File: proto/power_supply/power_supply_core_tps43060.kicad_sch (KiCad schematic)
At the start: 36 parts, among them Q1 BC846, U1 TPS61178, U2 TSV911xxLx

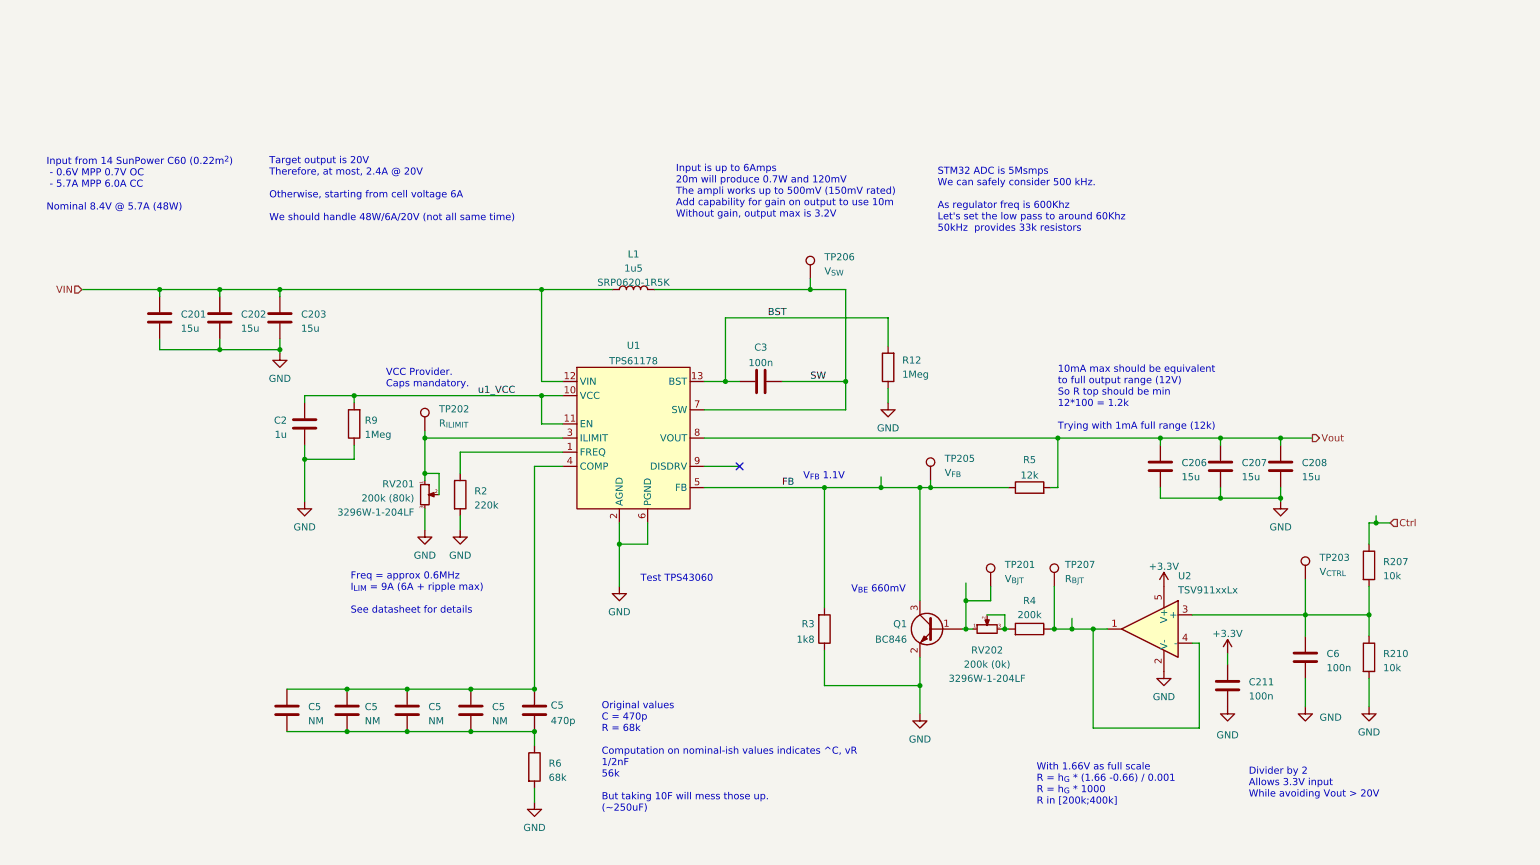
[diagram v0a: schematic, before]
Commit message: Global alimentation update
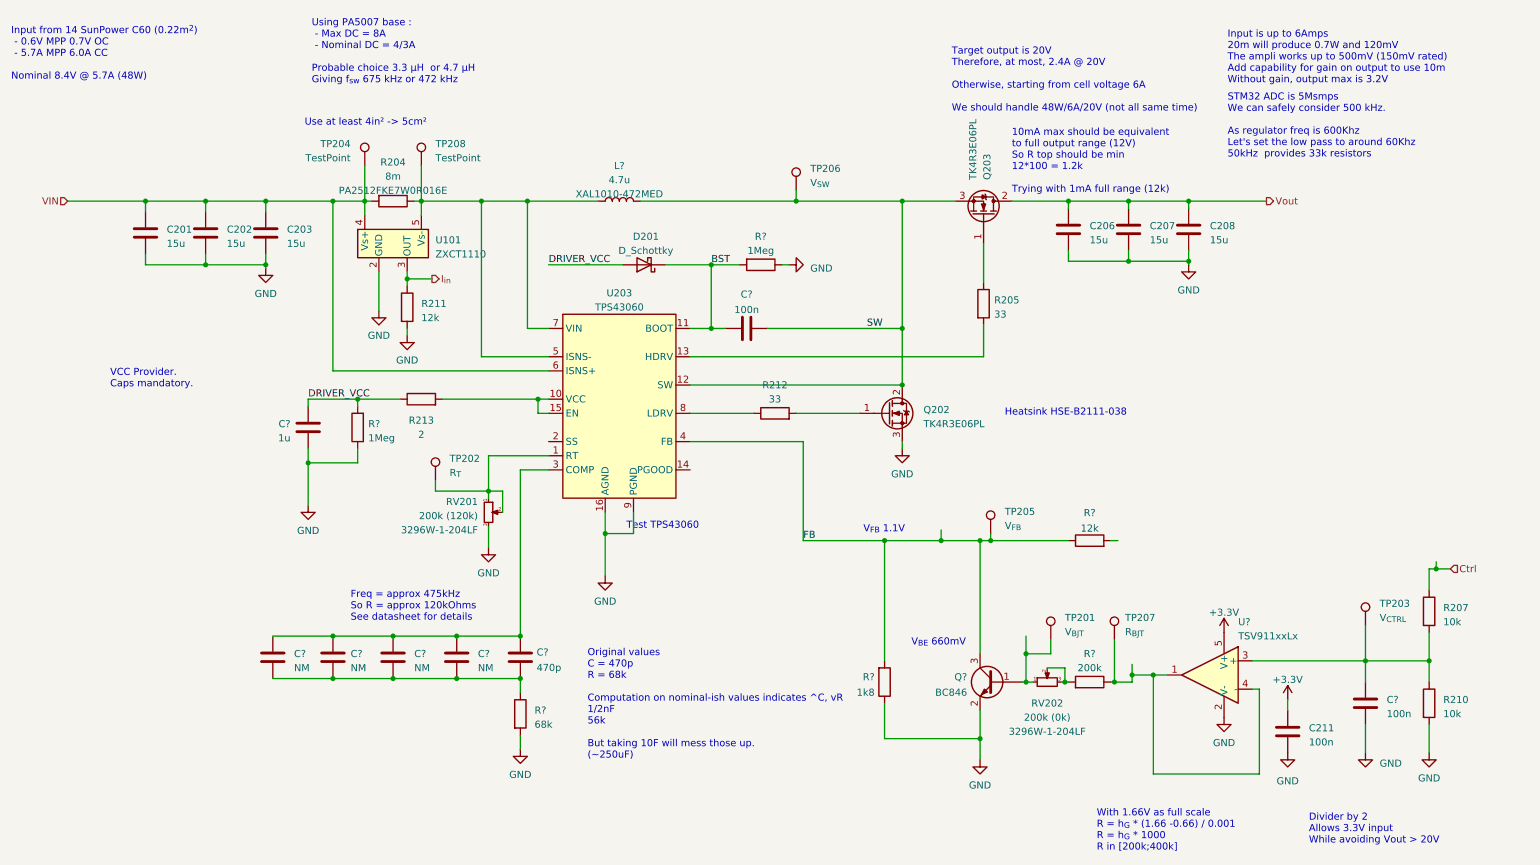
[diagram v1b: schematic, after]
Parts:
- removed R2: 220k, Resistor_SMD:R_0805_2012Metric, symbol Device:R
- removed U1: TPS61178, power_supply:VSON-TPS61178, symbol defis_solaires_4:TPS61178
- added D201: D_Schottky, symbol Device:D_Schottky
- added Q202, Q203: TK4R3E06PL, Package_TO_SOT_THT:TO-220-3_Horizontal_TabUp, symbol Device:Q_NMOS_GDS
- added R204: 8m, Resistor_SMD:R_2512_6332Metric, symbol Device:R
- added R205, R212: 33, symbol Device:R
- added R211: 12k, Resistor_SMD:R_0805_2012Metric, symbol Device:R
- added R213: 2, symbol Device:R
- added TP204, TP208: TestPoint, TestPoint:TestPoint_Keystone_5010-5014_Multipurpose, symbol Connector:TestPoint
- added U101: ZXCT1110, Package_TO_SOT_SMD:SOT-23-5, symbol Amplifier_Current:ZXCT1110
- added U203: TPS43060, power_supply:QFN-16_EP_3x3_Pitch0.5mm, symbol defis_solaires_4:TPS43060
- L?: renamed from L1; value 1u5 -> 4.7u; footprint power_supply:SRP0620 -> Inductor_SMD:L_Coilcraft_XAL1010-XXX; MPN SRP0620-1R5K -> XAL1010-472MED
- RV201: value 200k (80k) -> 200k (120k)
- TP202: value R_{ILIMIT} -> R_{T}
- renumbered C5 to C?, C6 to C?, C2 to C?, C3 to C?, Q1 to Q?, R4 to R?, R12 to R?, R3 to R?, R9 to R?, R5 to R?, R6 to R?, U2 to U?
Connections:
- net BST: now also D201.1 (K), U203.11 (BOOT)
- net FB: now also U203.4 (FB)
- net GND: now also Q202.3 (S), R211.2, U101.2 (GND), U203.16 (AGND), U203.9 (PGND)
- net SW: now also Q202.2 (D), Q203.3 (S), U203.12 (SW)
- net VIN: now also R204.2, TP204.1, U101.4 (Vs+), U203.6 (ISNS+); no longer L?.1
- net Vout: now also Q203.2 (D); no longer R?.2
- net at RV201.1, RV201.2, TP202.1: now also U203.1 (RT)
- net at C?.1, C?.1, C?.1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: now also U203.3 (COMP)
- net u1_VCC renamed DRIVER_VCC
- net DRIVER_VCC: now also D201.2 (A), R213.1
- new net: Q202.1 (G), R212.2
- new net: L?.1, R204.1, TP208.1, U101.5 (Vs-), U203.5 (ISNS-), U203.7 (VIN)
- new net: R212.1, U203.8 (LDRV)
- new net: Q203.1 (G), R205.1
- new net: R205.2, U203.13 (HDRV)
- new net: R213.2, U203.10 (VCC), U203.15 (EN)
- new net I_{in}: R211.1, U101.3 (OUT)
- no-connect marks 1 -> 0
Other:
- note added: "Freq = approx 475kHz So R = approx 120kOhms See datasheet for details"
- note added: "Heatsink HSE-B2111-038"
- note added: "Use at least 4in² -> 5cm²"
- note added: "Using PA5007 base : - Max DC = 8A - Nominal DC = 4/3A Probable choice 3.3 µH or 4.7 µH Giving f_{sw} 675 kHz or 472 kHz"
- note removed: "Freq = approx 0.6MHz I_{LIM} = 9A (6A + ripple max) See datasheet for details"
- moved on the sheet: C201, C202, C203, C206, C207, C208, C211, C?, L?, Q?, R207, R210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

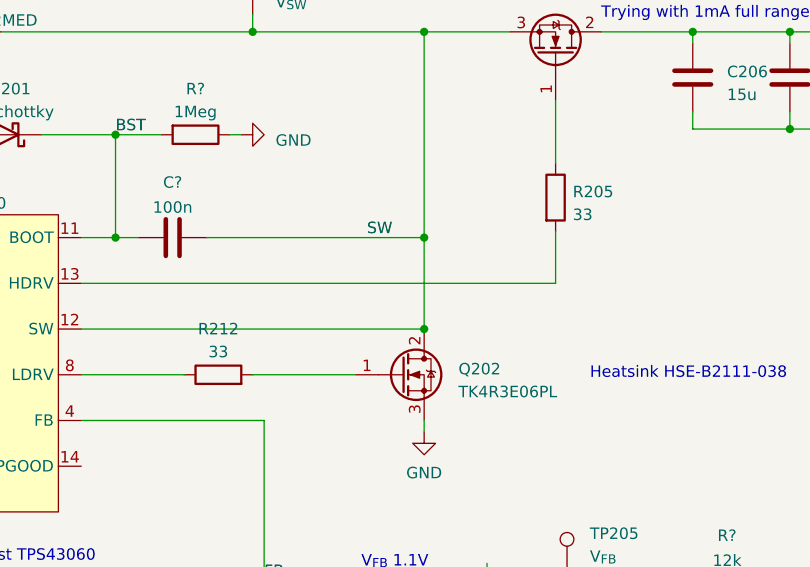
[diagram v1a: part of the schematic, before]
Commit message: Add maths for gate drive
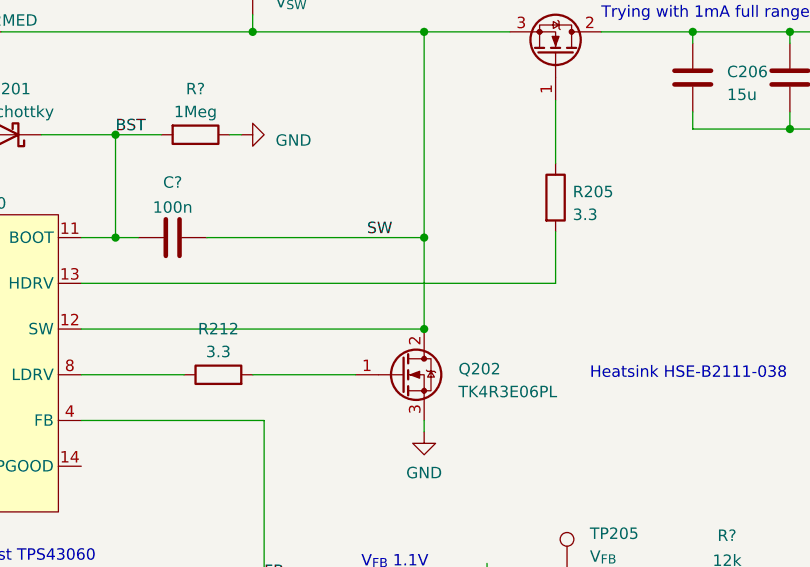
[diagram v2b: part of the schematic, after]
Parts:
- R205, R212: value 33 -> 3.3
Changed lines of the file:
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@@
       (effects (font (size 1.27 1.27)))
     )
-    (property "Value" "33" (at 156.21 82.55 90)
+    (property "Value" "3.3" (at 156.21 82.55 90)
       (effects (font (size 1.27 1.27)))
     )
@@
       (effects (font (size 1.27 1.27)) (justify left))
     )
-    (property "Value" "33" (at 195.58 67.31 0)
+    (property "Value" "3.3" (at 195.58 67.31 0)
       (effects (font (size 1.27 1.27)) (justify left))
     )

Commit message: Finish alim sch, start PCB
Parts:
- removed C? (x4): NM, Capacitor_SMD:C_0805_2012Metric, symbol Device:C
- removed R? (x2): 1Meg, Resistor_SMD:R_0805_2012Metric, symbol Device:R
- removed RV201: 200k (120k), Potentiometer_THT:Potentiometer_Bourns_3296W_Vertical, symbol Device:R_Potentiometer_Small
- removed TP202: R_{T}, TestPoint:TestPoint_Keystone_5010-5014_Multipurpose, symbol Connector:TestPoint
- added C204, C208, C209: 47u, Capacitor_SMD:C_1206_3216Metric, symbol Device:C
- added C215: 100n, Capacitor_SMD:C_0805_2012Metric, symbol Device:C
- added R208: 470k, Resistor_SMD:R_0805_2012Metric, symbol Device:R
- added R?: 150k, Resistor_SMD:R_0805_2012Metric, symbol Device:R
- C201, C202, C203: value 15u -> 47u; footprint Capacitor_SMD:C_0805_2012Metric -> Capacitor_SMD:C_1206_3216Metric
- C205: renamed from C206; value 15u -> 47u; footprint Capacitor_SMD:C_0805_2012Metric -> Capacitor_SMD:C_1206_3216Metric
- C206: renamed from C207; value 15u -> 47u; footprint Capacitor_SMD:C_0805_2012Metric -> Capacitor_SMD:C_1206_3216Metric
- C207: renamed from C208; value 15u -> 47u; footprint Capacitor_SMD:C_0805_2012Metric -> Capacitor_SMD:C_1206_3216Metric
- C?: value 470p -> 47n
- C?: value 100n -> 100n/16V
- D201: value D_Schottky -> XBS104S14R-G; footprint (none) -> Diode_SMD:D_SOD-123
- L?: value 4.7u -> 22u; footprint Inductor_SMD:L_Coilcraft_XAL1010-XXX -> Inductor_SMD:L_Coilcraft_XAL1510-223; MPN XAL1010-472MED -> XAL1510-223MED
- R203: renamed from R205; value 3.3 -> 2; footprint (none) -> Resistor_SMD:R_0805_2012Metric
- R205: renamed from R213; footprint (none) -> Resistor_SMD:R_0805_2012Metric
- R206: renamed from R212; value 3.3 -> 2; footprint (none) -> Resistor_SMD:R_0805_2012Metric
- R?: value 68k -> 15k
- renumbered C211 to C214, Q203 to Q201, R204 to R201, R211 to R204, R207 to R210, R210 to R213, RV202 to RV201, TP204 to TP201, TP208 to TP202, TP206 to TP203, TP205 to TP204, TP203 to TP205, TP201 to TP206, U203 to U202
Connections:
- net GND: now also C204.2, C208.2, C209.2, C215.2, R208.2, R?.2
- net VIN: no longer C203.1
- net Vout: now also C203.1, R?.2, C204.1, C208.1, C209.1
- net DRV_VIN: now reaches L?.1, R201.1, TP202.1, U101.5 (Vs-), U202.5 (ISNS-), U202.7 (VIN)
- net at U202.1 (RT): now also R208.1
- net at C?.2, R?.1: now also R?.1
- net at U202.2 (SS): now also C215.1
- no-connect marks 0 -> 1
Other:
- note added: "Computation shows : R = 13.7 kOhms C = 48 nF"
- note added: "Freq = approx 125kHz So R = approx 470kOhms Effective approx 122kHz See datasheet for details"
- note added: "V_{FB} 1.22V"
- note removed: "Freq = approx 475kHz So R = approx 120kOhms See datasheet for details"
- note removed: "Input is up to 6Amps 20m will produce 0.7W and 120mV The ampli works up to 500mV (150mV rated) Add capability for gain on output to use 10m Without gain, output max is 3.2V"
- note removed: "Original values C = 470p R = 68k Computation on nominal-ish values indicates ^C, vR 1/2nF 56k But taking 10F will mess those up. (~250uF)"
- note removed: "STM32 ADC is 5Msmps We can safely consider 500 kHz. As regulator freq is 600Khz Let's set the low pass to around 60Khz 50kHz provides 33k resistors"
- note removed: "V_{FB} 1.1V"
- moved on the sheet: C205, C206, C207

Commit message: Update PCB
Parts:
- added C216: 15p, Capacitor_SMD:C_0805_2012Metric, symbol Device:C
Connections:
- net DRV_VIN: no longer U202.7 (VIN)
- net FB: now also C216.1
- net GND: now also C216.2
- net VIN: now also U202.7 (VIN)
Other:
- note added: "Might be used to filter 50ns pulse of FET drive"
- note removed: "Using PA5007 base : - Max DC = 8A - Nominal DC = 4/3A Probable choice 3.3 µH or 4.7 µH Giving f_{sw} 675 kHz or 472 kHz"
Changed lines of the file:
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@@
   (junction (at 179.07 46.99) (diameter 0) (color 0 0 0 0)
   )
-  (junction (at 111.76 46.99) (diameter 0) (color 0 0 0 0)
+  (junction (at 161.29 107.95) (diameter 0) (color 0 0 0 0)
   )
   (junction (at 201.295 133.35) (diameter 0) (color 0 0 0 0)
@@
     (stroke (width 0) (type default))
   )
-  (wire (pts (xy 111.76 69.85) (xy 111.76 46.99))
-    (stroke (width 0) (type default))
-  )
   (wire (pts (xy 115.57 69.85) (xy 111.76 69.85))
     (stroke (width 0) (type default))
@@
     (stroke (width 0) (type default))
   )
-  (wire (pts (xy 111.76 46.99) (xy 124.46 46.99))
-    (stroke (width 0) (type default))
-  )
   (wire (pts (xy 241.3 56.515) (xy 241.3 58.42))
     (stroke (width 0) (type default))
@@
     (stroke (width 0) (type default))
   )
+  (wire (pts (xy 161.29 107.95) (xy 161.29 114.3))
+    (stroke (width 0) (type default))
+  )
   (wire (pts (xy 208.28 46.99) (xy 219.075 46.99))
     (stroke (width 0) (type default))
@@
     (stroke (width 0) (type default))
   )
-  (wire (pts (xy 103.505 46.99) (xy 111.76 46.99))
+  (wire (pts (xy 103.505 46.99) (xy 124.46 46.99))
     (stroke (width 0) (type default))
   )
@@
     (effects (font (size 1.27 1.27)) (justify left bottom))
   )
+  (text "Might be used to filter\n50ns pulse of FET drive" (at 157.48 119.38 0)
+    (effects (font (size 1.27 1.27)) (justify right bottom))
+  )
   (text "VCC Provider.\nCaps mandatory." (at 36.83 80.645 0)
     (effects (font (size 1.27 1.27)) (justify left bottom))
@@
   (text "Freq = approx 125kHz\nSo R = approx 470kOhms \nEffective approx 122kHz\nSee datasheet for details"
     (at 80.01 122.555 0)
-    (effects (font (size 1.27 1.27)) (justify left bottom))
-  )
-  (text "Using PA5007 base :\n - Max DC = 8A\n - Nominal DC = 4/3A\n\nProbable choice 3.3 µH  or 4.7 µH\nGiving f_{sw} 675 kHz or 472 kHz"
-    (at 73.025 26.035 0)
     (effects (font (size 1.27 1.27)) (justify left bottom))
   )
@@
     )
   )
+  (hierarchical_label "VIN" (shape input) (at 111.76 69.85 180) (fields_autoplaced)
+    (effects (font (size 1.27 1.27)) (justify right))
+  )
   (hierarchical_label "I_{in}" (shape output) (at 94.615 60.96 0) (fields_autoplaced)
     (effects (font (size 1.27 1.27)) (justify left))
@@
         (path "/e87df9ac-84db-475c-955a-f1fa477bbb69/91eacb21-145b-4d7f-8dcd-2105a1b91924"
           (reference "R203") (unit 1)
+        )
+      )
+    )
+  )
+  (symbol (lib_name "GND_4") (lib_id "power:GND") (at 161.29 121.92 0) (unit 1)
+    (in_bom yes) (on_board yes) (dnp no) (fields_autoplaced)
+    (property "Reference" "#PWR01" (at 161.29 128.27 0)
+      (effects (font (size 1.27 1.27)) hide)
+    )
+    (property "Value" "GND" (at 161.29 127 0)
+      (effects (font (size 1.27 1.27)))
+    )
+    (property "Footprint" "" (at 161.29 121.92 0)
+      (effects (font (size 1.27 1.27)) hide)
+    )
+    (property "Datasheet" "" (at 161.29 121.92 0)
+      (effects (font (size 1.27 1.27)) hide)
+    )
+    (pin "1")
+    (instances
+      (project "power_supply"
+        (path "/e87df9ac-84db-475c-955a-f1fa477bbb69/91eacb21-145b-4d7f-8dcd-2105a1b91924"
+          (reference "#PWR01") (unit 1)
         )
       )
@@
         )
       )
+    )
+  )
+  (symbol (lib_id "Device:C") (at 161.29 118.11 0) (unit 1)
+    (in_bom yes) (on_board yes) (dnp no) (fields_autoplaced)
+    (property "Reference" "C216" (at 165.1 117.475 0)
+      (effects (font (size 1.27 1.27)) (justify left))
+    )
+    (property "Value" "15p" (at 165.1 120.015 0)
+      (effects (font (size 1.27 1.27)) (justify left))
+    )
+    (property "Footprint" "Capacitor_SMD:C_0805_2012Metric" (at 162.2552 121.92 0)
+      (effects (font (size 1.27 1.27)) hide)
+    )
+    (property "Datasheet" "~" (at 161.29 118.11 0)
+      (effects (font (size 1.27 1.27)) hide)
+    )
+    (pin "1")
+    (pin "2")
+    (instances
+      (project "power_supply"
+        (path "/e87df9ac-84db-475c-955a-f1fa477bbb69/91eacb21-145b-4d7f-8dcd-2105a1b91924"
+          (reference "C216") (unit 1)
+        )
+      )

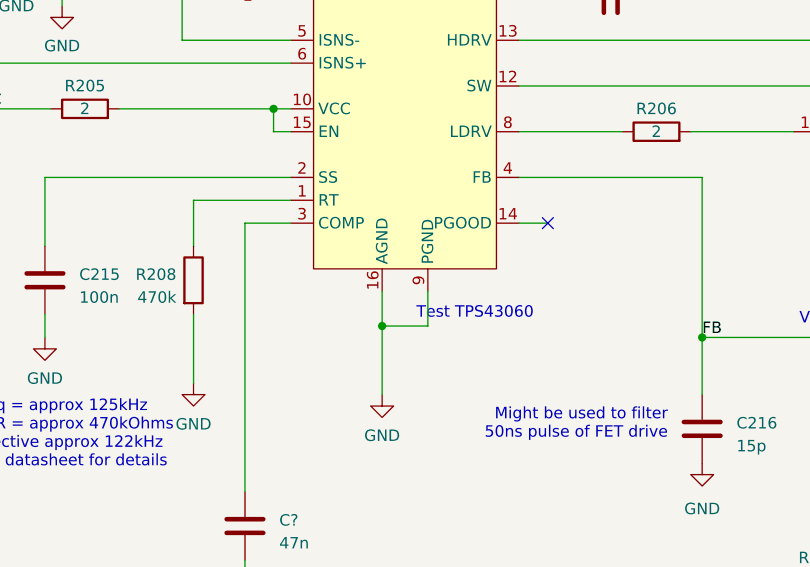
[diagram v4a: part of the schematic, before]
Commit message: Finish first routing
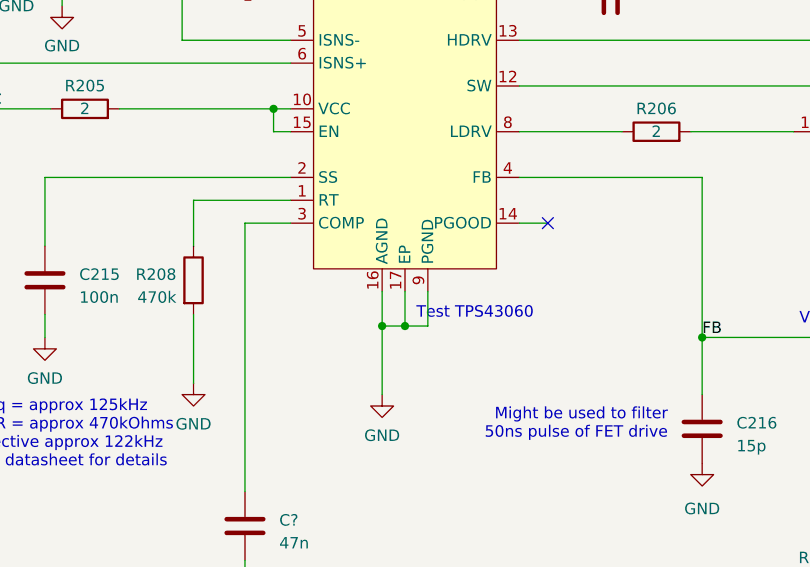
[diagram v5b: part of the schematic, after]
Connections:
- net GND: now also U202.17 (EP)
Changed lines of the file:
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@@
   (junction (at 262.89 46.99) (diameter 0) (color 0 0 0 0)
+  )
+  (junction (at 128.27 106.68) (diameter 0) (color 0 0 0 0)
   )
   (junction (at 274.955 113.03) (diameter 0) (color 0 0 0 0)
@@
     (stroke (width 0) (type default))
   )
+  (wire (pts (xy 128.27 102.87) (xy 128.27 106.68))
+    (stroke (width 0) (type default))
+  )
   (wire (pts (xy 216.535 133.35) (xy 217.17 133.35))
     (stroke (width 0) (type default))
@@
     (stroke (width 0) (type default))
   )
+  (wire (pts (xy 128.27 106.68) (xy 125.73 106.68))
+    (stroke (width 0) (type default))
+  )
   (wire (pts (xy 241.935 134.62) (xy 243.205 134.62))
     (stroke (width 0) (type default))
@@
     (stroke (width 0) (type default))
   )
-  (wire (pts (xy 130.81 106.68) (xy 125.73 106.68))
+  (wire (pts (xy 130.81 106.68) (xy 128.27 106.68))
     (stroke (width 0) (type default))
   )
@@
     (pin "15")
     (pin "16")
+    (pin "17")
     (pin "2")
     (pin "3")
